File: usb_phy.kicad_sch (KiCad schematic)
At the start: 14 parts, among them U8 USB3343-CP

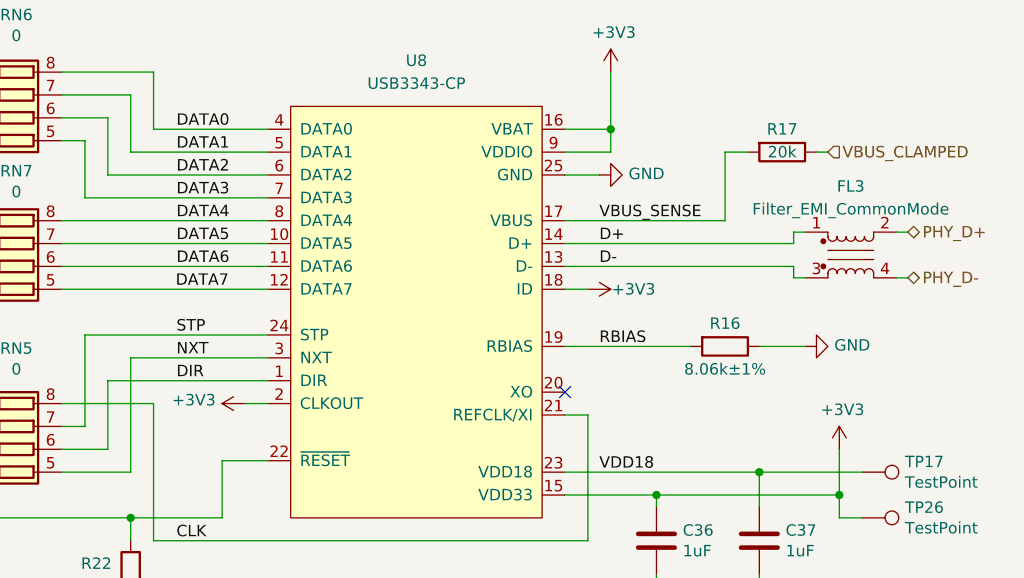
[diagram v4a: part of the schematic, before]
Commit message: Add second common-mode choke for TARGET port
Instead of having a single choke connected in series with the PHY, we
now have a choke in series with each connector. The PHY is connected
between the two chokes.
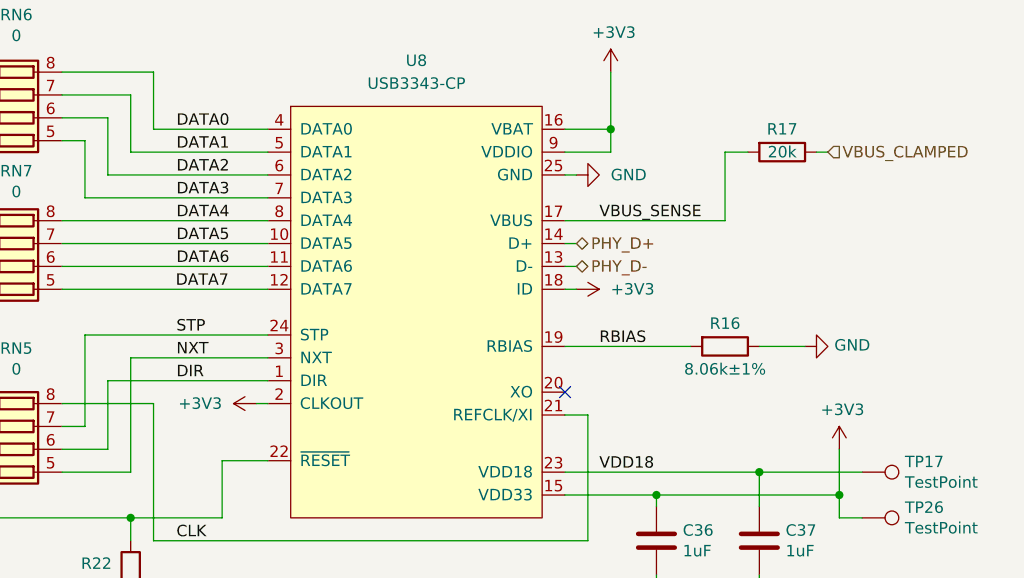
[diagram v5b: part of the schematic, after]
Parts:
- removed FL3: Filter_EMI_CommonMode, cynthion:L_CommonModeChoke_Murata_DLM0NS, symbol Device:Filter_EMI_CommonMode
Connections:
- net D+ is gone; now on net PHY_D+: U8.14 (D+)
- net D- is gone; now on net PHY_D-: U8.13 (D-)
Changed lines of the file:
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@@
-    (stroke (width 0) (type default))
-  )
-  (wire (pts (xy 199.39 71.12) (xy 200.66 71.12))
     (stroke (width 0) (type default))
   )
@@
     (stroke (width 0) (type default))
   )
-  (wire (pts (xy 173.99 74.93) (xy 199.39 74.93))
+  (wire (pts (xy 173.99 74.93) (xy 175.26 74.93))
     (stroke (width 0) (type default))
   )
@@
     (stroke (width 0) (type default))
   )
-  (wire (pts (xy 173.99 77.47) (xy 176.53 77.47))
+  (wire (pts (xy 173.99 77.47) (xy 175.26 77.47))
     (stroke (width 0) (type default))
   )
@@
     (stroke (width 0) (type default))
   )
-  (wire (pts (xy 199.39 74.93) (xy 199.39 76.2))
-    (stroke (width 0) (type default))
-  )
   (wire (pts (xy 125.73 85.09) (xy 125.73 97.79))
     (stroke (width 0) (type default))
@@
     (stroke (width 0) (type default))
   )
-  (wire (pts (xy 173.99 64.77) (xy 177.8 64.77))
+  (wire (pts (xy 173.99 64.77) (xy 175.26 64.77))
     (stroke (width 0) (type default))
   )
@@
     (stroke (width 0) (type default))
   )
-  (wire (pts (xy 212.09 76.2) (xy 210.82 76.2))
-    (stroke (width 0) (type default))
-  )
   (wire (pts (xy 154.94 160.02) (xy 154.94 161.29))
     (stroke (width 0) (type default))
@@
     (stroke (width 0) (type default))
   )
-  (wire (pts (xy 199.39 72.39) (xy 199.39 71.12))
-    (stroke (width 0) (type default))
-  )
   (wire (pts (xy 191.77 69.85) (xy 191.77 62.23))
     (stroke (width 0) (type default))
@@
     (stroke (width 0) (type default))
   )
-  (wire (pts (xy 210.82 71.12) (xy 212.09 71.12))
-    (stroke (width 0) (type default))
-  )
   (wire (pts (xy 173.99 91.44) (xy 176.53 91.44))
     (stroke (width 0) (type default))
   )
-  (wire (pts (xy 199.39 76.2) (xy 200.66 76.2))
-    (stroke (width 0) (type default))
-  )
   (wire (pts (xy 195.58 101.6) (xy 195.58 97.79))
     (stroke (width 0) (type default))
@@
     (stroke (width 0) (type default))
   )
-  (wire (pts (xy 140.97 90.17) (xy 138.43 90.17))
+  (wire (pts (xy 140.97 90.17) (xy 139.7 90.17))
     (stroke (width 0) (type default))
   )
@@
     (stroke (width 0) (type default))
   )
-  (wire (pts (xy 173.99 72.39) (xy 199.39 72.39))
+  (wire (pts (xy 173.99 72.39) (xy 175.26 72.39))
     (stroke (width 0) (type default))
   )
@@
     (effects (font (size 1.27 1.27)) (justify left bottom))
   )
-  (label "D+" (at 177.8 72.39 0) (fields_autoplaced)
-    (effects (font (size 1.27 1.27)) (justify left bottom))
-  )
   (label "PHY.STP" (at 92.71 92.71 0) (fields_autoplaced)
     (effects (font (size 1.27 1.27)) (justify left bottom))
@@
   )
   (label "DATA1" (at 130.81 62.23 0) (fields_autoplaced)
-    (effects (font (size 1.27 1.27)) (justify left bottom))
-  )
-  (label "D-" (at 177.8 74.93 0) (fields_autoplaced)
     (effects (font (size 1.27 1.27)) (justify left bottom))
   )
@@
     (effects (font (size 1.27 1.27)) (justify right))
   )
-  (hierarchical_label "PHY_D-" (shape bidirectional) (at 212.09 76.2 0) (fields_autoplaced)
+  (hierarchical_label "PHY_D-" (shape bidirectional) (at 175.26 74.93 0) (fields_autoplaced)
     (effects (font (size 1.27 1.27)) (justify left))
   )
@@
     (effects (font (size 1.27 1.27)) (justify left))
   )
-  (hierarchical_label "PHY_D+" (shape bidirectional) (at 212.09 71.12 0) (fields_autoplaced)
+  (hierarchical_label "PHY_D+" (shape bidirectional) (at 175.26 72.39 0) (fields_autoplaced)
     (effects (font (size 1.27 1.27)) (justify left))
   )
@@
     )
   )
-  (symbol (lib_id "power:GND") (at 177.8 64.77 90) (unit 1)
-    (in_bom yes) (on_board yes) (dnp no)
-    (property "Reference" "#PWR059" (at 184.15 64.77 0)
-      (effects (font (size 1.27 1.27)) hide)
-    )
-    (property "Value" "GND" (at 181.0512 64.643 90)
+  (symbol (lib_id "power:GND") (at 175.26 64.77 90) (unit 1)
+    (in_bom yes) (on_board yes) (dnp no) (fields_autoplaced)
+    (property "Reference" "#PWR059" (at 181.61 64.77 0)
+      (effects (font (size 1.27 1.27)) hide)
+    )
+    (property "Value" "GND" (at 179.07 64.77 90)
       (effects (font (size 1.27 1.27)) (justify right))
     )
-    (property "Footprint" "" (at 177.8 64.77 0)
-      (effects (font (size 1.27 1.27)) hide)
-    )
-    (property "Datasheet" "" (at 177.8 64.77 0)
+    (property "Footprint" "" (at 175.26 64.77 0)
+      (effects (font (size 1.27 1.27)) hide)
+    )
+    (property "Datasheet" "" (at 175.26 64.77 0)
       (effects (font (size 1.27 1.27)) hide)
     )
@@
     )
   )
-  (symbol (lib_id "Device:Filter_EMI_CommonMode") (at 205.74 73.66 0) (unit 1)
-    (in_bom yes) (on_board yes) (dnp no)
-    (property "Reference" "FL3" (at 205.74 66.04 0)
-      (effects (font (size 1.27 1.27)))
-    )
-    (property "Value" "Filter_EMI_CommonMode" (at 205.74 68.5769 0)
-      (effects (font (size 1.27 1.27)))
-    )
-    (property "Footprint" "cynthion:L_CommonModeChoke_Murata_DLM0NS" (at 205.74 72.644 0)
-      (effects (font (size 1.27 1.27)) hide)
-    )
-    (property "Datasheet" "https://www.murata.com/en-global/products/productdata/8799424610334/EFLD0009.pdf" (at 205.74 72.644 0)
-      (effects (font (size 1.27 1.27)) hide)
-    )
-    (property "Description" "CMC 130MA 2LN 28 OHM SMD" (at 205.74 73.66 0)
-      (effects (font (size 1.27 1.27)) hide)
-    )
-    (property "Manufacturer" "Murata" (at 205.74 73.66 0)
-      (effects (font (size 1.27 1.27)) hide)
-    )
-    (property "Part Number" "DLM0NSB280HY2D" (at 205.74 73.66 0)
-      (effects (font (size 1.27 1.27)) hide)
-    )
-    (pin "1")
-    (pin "2")
-    (pin "3")
-    (pin "4")
-    (instances
-      (project "cynthion"
-        (path "/fb621148-8145-4217-9712-738e1b5a4823/00000000-0000-0000-0000-00005dcd9772/86be2f0e-7bb1-42d8-87bc-4230c6dbd013"
-          (reference "FL3") (unit 1)
-        )
-        (path "/fb621148-8145-4217-9712-738e1b5a4823/00000000-0000-0000-0000-00005dd754d4/6ef06f1e-62a2-438c-8ab4-363586d03e74"
-          (reference "FL1") (unit 1)
-        )
-        (path "/fb621148-8145-4217-9712-738e1b5a4823/00000000-0000-0000-0000-00005dddb747/6fe66c21-f87e-45b5-9c98-390633af1111"
-          (reference "FL2") (unit 1)
-        )
-      )
-    )
-  )
   (symbol (lib_id "power:+3V3") (at 204.47 95.25 0) (unit 1)
     (in_bom yes) (on_board yes) (dnp no)
@@
     )
   )
-  (symbol (lib_id "power:+3V3") (at 176.53 77.47 270) (unit 1)
-    (in_bom yes) (on_board yes) (dnp no)
-    (property "Reference" "#PWR061" (at 172.72 77.47 0)
-      (effects (font (size 1.27 1.27)) hide)
-    )
-    (property "Value" "+3V3" (at 181.61 77.47 90)
-      (effects (font (size 1.27 1.27)))
-    )
-    (property "Footprint" "" (at 176.53 77.47 0)
-      (effects (font (size 1.27 1.27)) hide)
-    )
-    (property "Datasheet" "" (at 176.53 77.47 0)
+  (symbol (lib_id "power:+3V3") (at 175.26 77.47 270) (unit 1)
+    (in_bom yes) (on_board yes) (dnp no) (fields_autoplaced)
+    (property "Reference" "#PWR061" (at 171.45 77.47 0)
+      (effects (font (size 1.27 1.27)) hide)
+    )
+    (property "Value" "+3V3" (at 179.07 77.47 90)
+      (effects (font (size 1.27 1.27)) (justify left))
+    )
+    (property "Footprint" "" (at 175.26 77.47 0)
+      (effects (font (size 1.27 1.27)) hide)
+    )
+    (property "Datasheet" "" (at 175.26 77.47 0)
       (effects (font (size 1.27 1.27)) hide)
     )
@@
     )
   )
-  (symbol (lib_id "power:+3V3") (at 138.43 90.17 90) (unit 1)
-    (in_bom yes) (on_board yes) (dnp no)
-    (property "Reference" "#PWR063" (at 142.24 90.17 0)
-      (effects (font (size 1.27 1.27)) hide)
-    )
-    (property "Value" "+3V3" (at 135.1788 89.789 90)
-      (effects (font (size 1.27 1.27)) (justify left))
-    )
-    (property "Footprint" "" (at 138.43 90.17 0)
-      (effects (font (size 1.27 1.27)) hide)
-    )
-    (property "Datasheet" "" (at 138.43 90.17 0)
-      (effects (font (size 1.27 1.27)) hide)
-    )
+  (symbol (lib_id "power:+3V3") (at 139.7 90.17 90) (unit 1)
+    (in_bom yes) (on_board yes) (dnp no) (fields_autoplaced)
+    (property "Reference" "#PWR063" (at 143.51 90.17 0)
+      (effects (font (size 1.27 1.27)) hide)
+    )
+    (property "Value" "+3V3" (at 135.89 90.17 90)
+      (effects (font (size 1.27 1.27)) (justify left))
+    )
+    (property "Footprint" "" (at 139.7 90.17 0)
+      (effects (font (size 1.27 1.27)) hide)
+    )
+    (property "Datasheet" "" (at 139.7 90.17 0)
+      (effects (font (size 1.27 1.27)) hide)
+    )

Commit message: Update copyright notices
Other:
- company: Copyright 2019-2023 Great Scott Gadgets -> ${COPYRIGHT}
- title: Cynthion -> ${TITLE}
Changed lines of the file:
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@@
   (paper "A4")
   (title_block
-    (title "Cynthion")
+    (title "${TITLE}")
     (date "${DATE}")
     (rev "${VERSION}")
-    (company "Copyright 2019-2023 Great Scott Gadgets")
-    (comment 1 "Licensed under the CERN-OHL-P v2")
+    (company "${COPYRIGHT}")
+    (comment 1 "${LICENSE}")
   )
   (junction (at 179.07 59.69) (diameter 0) (color 0 0 0 0)
